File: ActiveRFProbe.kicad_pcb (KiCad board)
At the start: 2 copper layers, 53 x 19 mm, 41 parts, among them J1 Conn_01x01, J16 Conn_01x01, J17 Conn_01x01, J18 Conn_01x01, J19 Conn_01x01, J2 Conn_01x01, J20 Conn_01x01, J21 Conn_01x01, J22 Conn_01x01, J23 Conn_01x01, J24 Conn_01x01, J25 Conn_Coaxial, J3 Conn_01x01, Q1 2SC4083, Q2 2SC4083, Q3 2SC4083

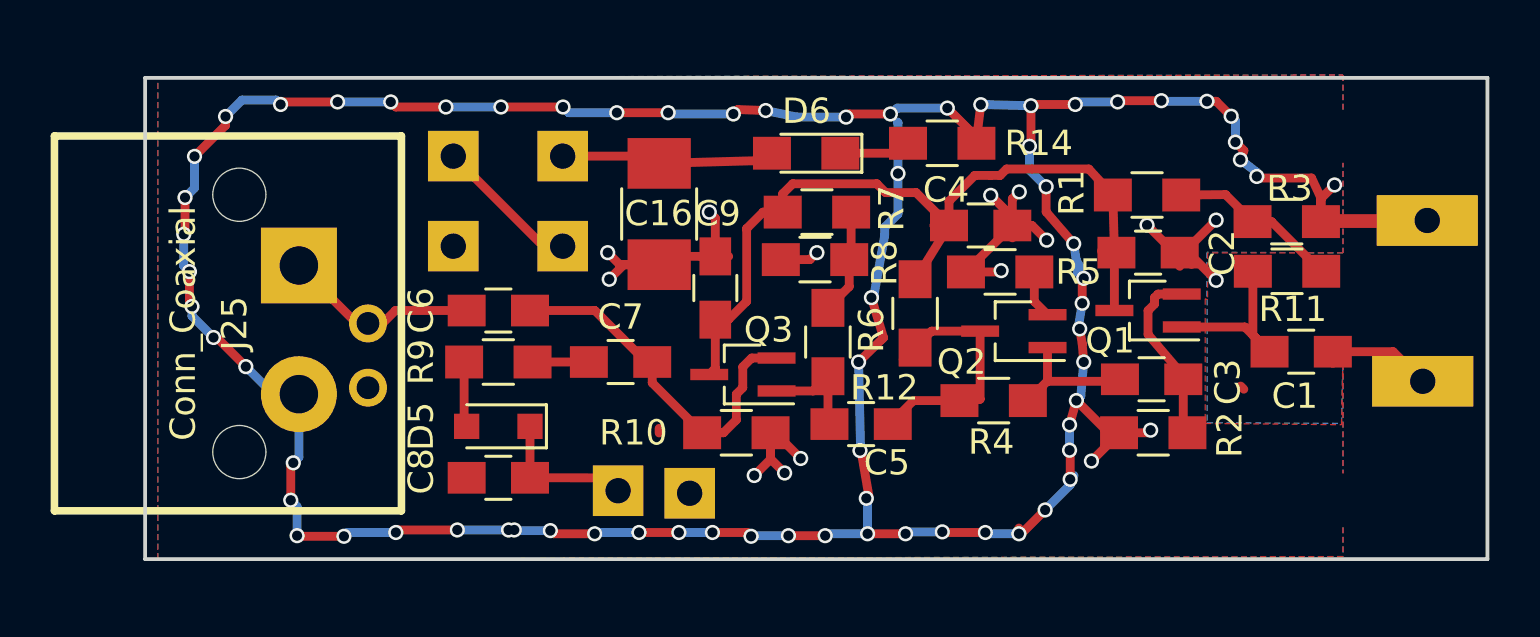
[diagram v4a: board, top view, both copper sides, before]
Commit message: Changed transistor to 2SC3357
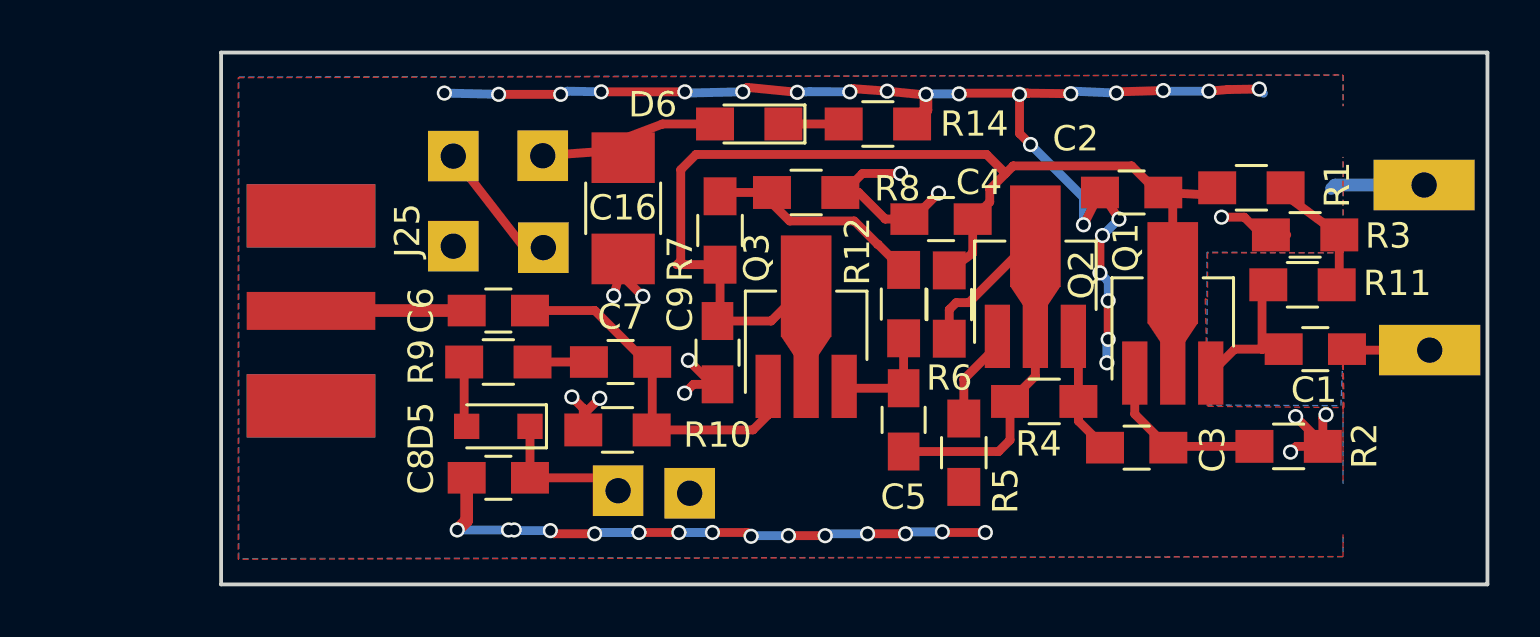
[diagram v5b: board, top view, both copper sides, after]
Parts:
- C1: value 10 nF -> 100 pF
- J25: footprint ActiveRFProbe:bnc_90_1-1337543-0_pad_combo -> ActiveRFProbe:Amphenol_RF_SMA_132289
- Q1, Q2, Q3: value 2SC4083 -> 2SC3357; footprint TO_SOT_Packages_SMD:SOT-323_SC-70_Handsoldering -> TO_SOT_Packages_SMD:SOT-89-3_Handsoldering
- moved J25 10.1 mm to (68.5, 91.2), turned to 180 degrees
- moved R5 7.28 mm to (94.3, 96.8), turned to 90 degrees
- moved R2 5.37 mm to (107.2, 96.5), turned to 0 degrees
- moved R10 4.70 mm to (80.7, 95.9), turned to 180 degrees
- moved R1 4.13 mm to (105.7, 86.3)
- moved R7 3.89 mm to (84.7, 88.0), turned to 90 degrees
- moved R12 3.34 mm to (91.9, 90.9)
- moved Q3 2.92 mm to (88.1, 92.2), turned to 90 degrees
- moved C3 2.76 mm to (101.2, 96.6)
- moved R8 2.67 mm to (88.1, 86.5), turned to 0 degrees
- moved R14 2.65 mm to (90.9, 83.8)
- moved C9 2.55 mm to (84.6, 92.8), turned to 90 degrees
- moved D6 2.53 mm to (85.9, 83.8)
- moved C2 2.46 mm to (101.0, 86.5), turned to 0 degrees
- moved R4 2.00 mm to (97.5, 94.8)
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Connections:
- Q1 pad 1: Net-(C1-Pad1) -> Net-(C3-Pad2)
- Q1 pad 2: Net-(C3-Pad2) -> +9V
- Q1 pad 3: +9V -> Net-(C1-Pad1)
- Q2 pad 1: Net-(C3-Pad1) -> Net-(Q2-Pad1)
- Q2 pad 2: Net-(Q2-Pad2) -> Net-(C5-Pad2)
- Q2 pad 3: Net-(C5-Pad2) -> Net-(C3-Pad1)
- Q3 pad 1: Net-(C5-Pad1) -> Net-(C6-Pad2)
- Q3 pad 2: Net-(C6-Pad2) -> +9V
- Q3 pad 3: +9V -> Net-(C5-Pad1)
- R5 pad 2: Net-(Q2-Pad2) -> Net-(Q2-Pad1)
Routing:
- net GND: track 188.1 -> 104.5 mm, vias 86 -> 52
- net +9V: track 34.3 -> 52.8 mm
- net Net-(C5-Pad2): track 10.4 -> 18.8 mm
- net Net-(Q2-Pad1): track 0.00 -> 5.16 mm
- net Net-(R12-Pad2): track 4.16 -> 8.83 mm
- net Net-(C1-Pad1): track 7.91 -> 5.91 mm
- net Net-(Q2-Pad2): track 1.90 -> 0.00 mm
- net Net-(R1-Pad2): track 6.78 -> 4.94 mm
- net Net-(C6-Pad1): track 7.78 -> 6.15 mm
- net Net-(C3-Pad1): track 6.34 -> 4.91 mm
- net Net-(C1-Pad2): track 4.50 -> 3.28 mm
- net Net-(C3-Pad2): track 7.99 -> 6.91 mm
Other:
- board size 53 x 19 mm -> 50 x 21 mm

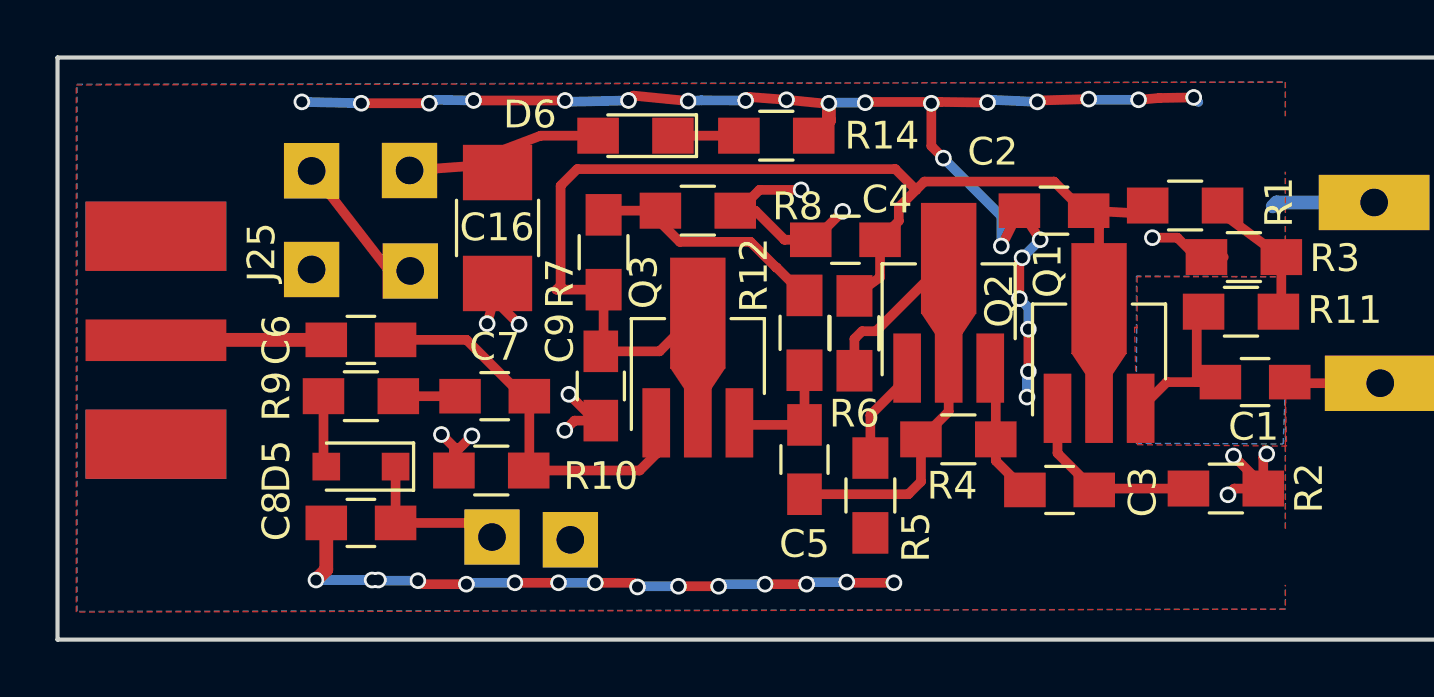
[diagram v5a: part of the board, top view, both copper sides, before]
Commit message: Fixed edge detector
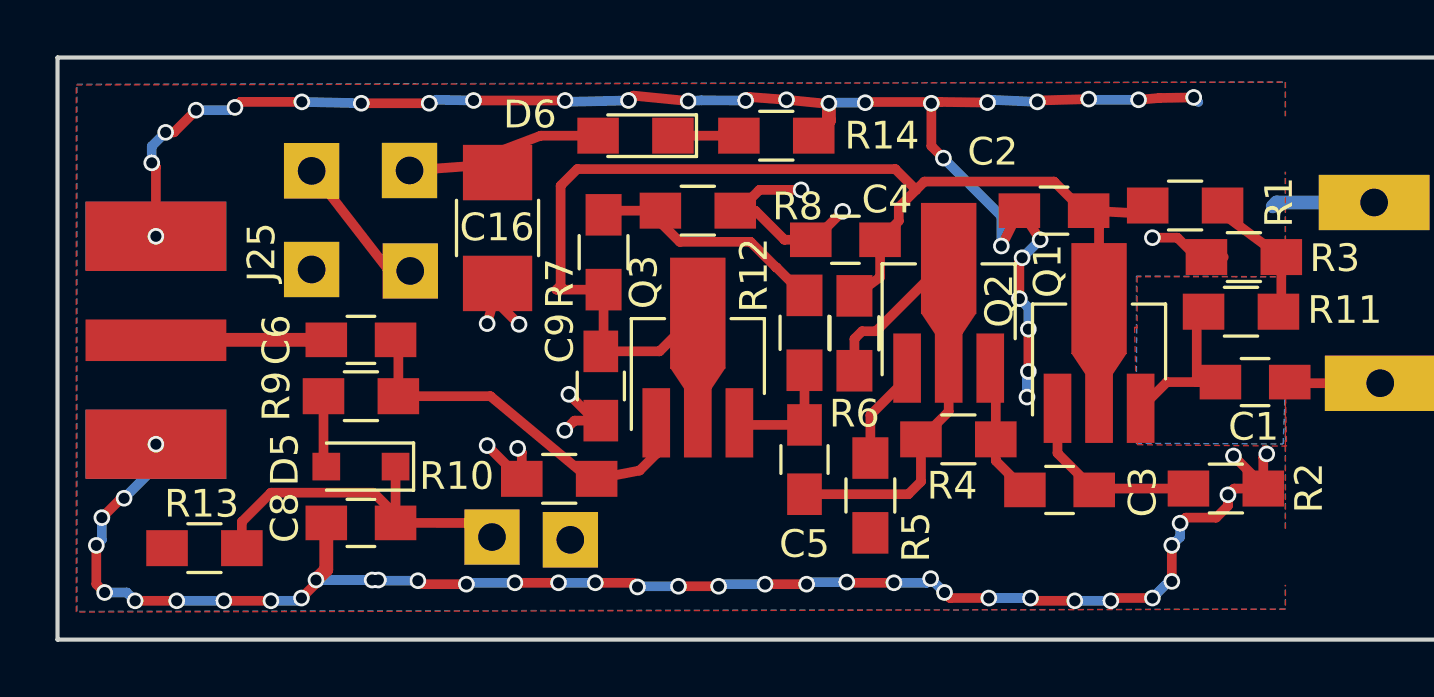
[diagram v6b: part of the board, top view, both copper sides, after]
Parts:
- removed C7: 10 nF, Capacitors_SMD:C_0805_HandSoldering
- added R13: 10k, Resistors_SMD:R_0805_HandSoldering, F.Cu at (70.3, 98.7)
- moved R10 2.47 mm to (83.1, 96.2)
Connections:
- R9 pad 2: Net-(C7-Pad1) -> Net-(C6-Pad2)
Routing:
- net GND: track 104.5 -> 143.7 mm, vias 52 -> 77
- net Net-(C8-Pad2): track 5.72 -> 13.3 mm
- net Net-(C7-Pad1): track 2.86 -> 0.00 mm

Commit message: Cleaned up the layout
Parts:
- removed R1, R3: 10k, Resistors_SMD:R_0805_HandSoldering
- removed R7, R8: 1k, Resistors_SMD:R_0805_HandSoldering
- R11: value 10k -> 47k
- R12: value 1k -> 47k
- R5: value 0R -> 47R
- R6: value 220R -> 100R
- moved J23 14.3 mm to (87.9, 83.8)
- moved J21 14.1 mm to (88.0, 98.9)
- moved J20 13.1 mm to (95.2, 98.8)
- moved J22 12.7 mm to (95.5, 83.9)
- moved R14 9.46 mm to (81.6, 85.3), turned to 180 degrees
- moved R2 4.95 mm to (102.4, 97.8), turned to 270 degrees
- moved C9 4.60 mm to (84.7, 88.2), turned to 0 degrees
- moved R6 4.31 mm to (97.8, 89.5)
- moved D6 4.21 mm to (81.7, 83.6)
- moved C5 3.95 mm to (90.7, 91.8)
- moved R12 3.77 mm to (89.3, 88.2), turned to 180 degrees
- moved C16 3.65 mm to (80.7, 90.8)
- moved Q2 3.11 mm to (94.4, 91.6)
- moved C4 2.86 mm to (96.0, 86.4)
- moved R11 2.69 mm to (105.2, 89.0), turned to 90 degrees
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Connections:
- C16 pad 2: Net-(C16-Pad2) -> +9V
- D6 pad 2: Net-(C16-Pad2) -> +9V
- J2 pad 1: Net-(C16-Pad2) -> +9V
- R11 pad 2: Net-(R1-Pad2) -> +9V
- R12 pad 2: Net-(R12-Pad2) -> +9V
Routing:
- net +9V: track 52.8 -> 75.0 mm
- net GND: track 143.7 -> 124.5 mm, vias 77 -> 70
- net Net-(R12-Pad2): track 8.83 -> 0.00 mm
- net Net-(C16-Pad2): track 8.59 -> 0.00 mm
- net Net-(C5-Pad1): track 4.35 -> 9.39 mm
- net Net-(R1-Pad2): track 4.94 -> 0.00 mm
- net Net-(C5-Pad2): track 18.8 -> 15.7 mm
- net Net-(C3-Pad1): track 4.91 -> 7.60 mm
- net Net-(C3-Pad2): track 6.91 -> 5.11 mm
- net Net-(Q2-Pad1): track 5.16 -> 4.12 mm
- net Net-(D6-Pad1): track 2.38 -> 1.77 mm
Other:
- board size 50 x 21 mm -> 49 x 22 mm
- board text added: "ACTIVE RF PROBE BY D MARKS KW4TI CC-BY-SA 4.0"
- board text removed: "RF PROBE BY D MARKS KW4TI CC-BY-SA 4.0"

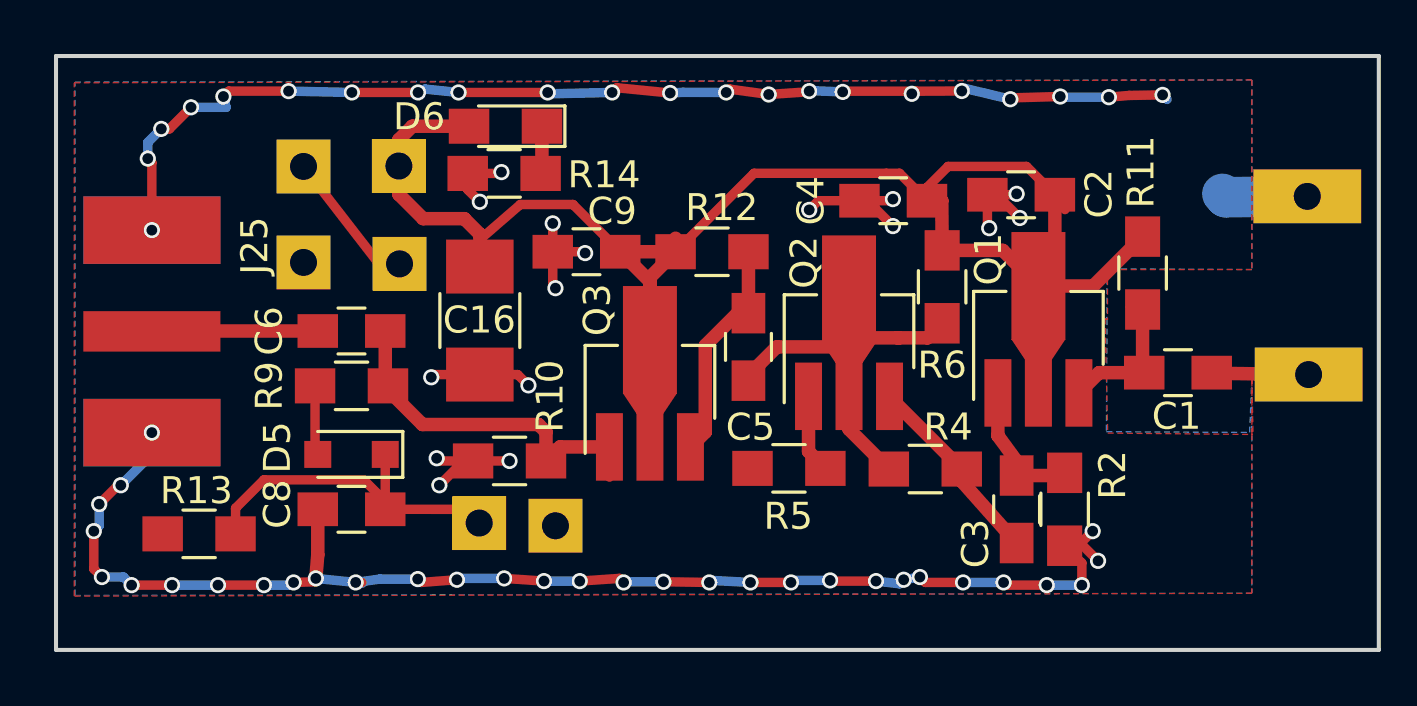
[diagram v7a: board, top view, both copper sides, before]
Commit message: Added LCSC parts, fixed symbol, added decoupling resistors
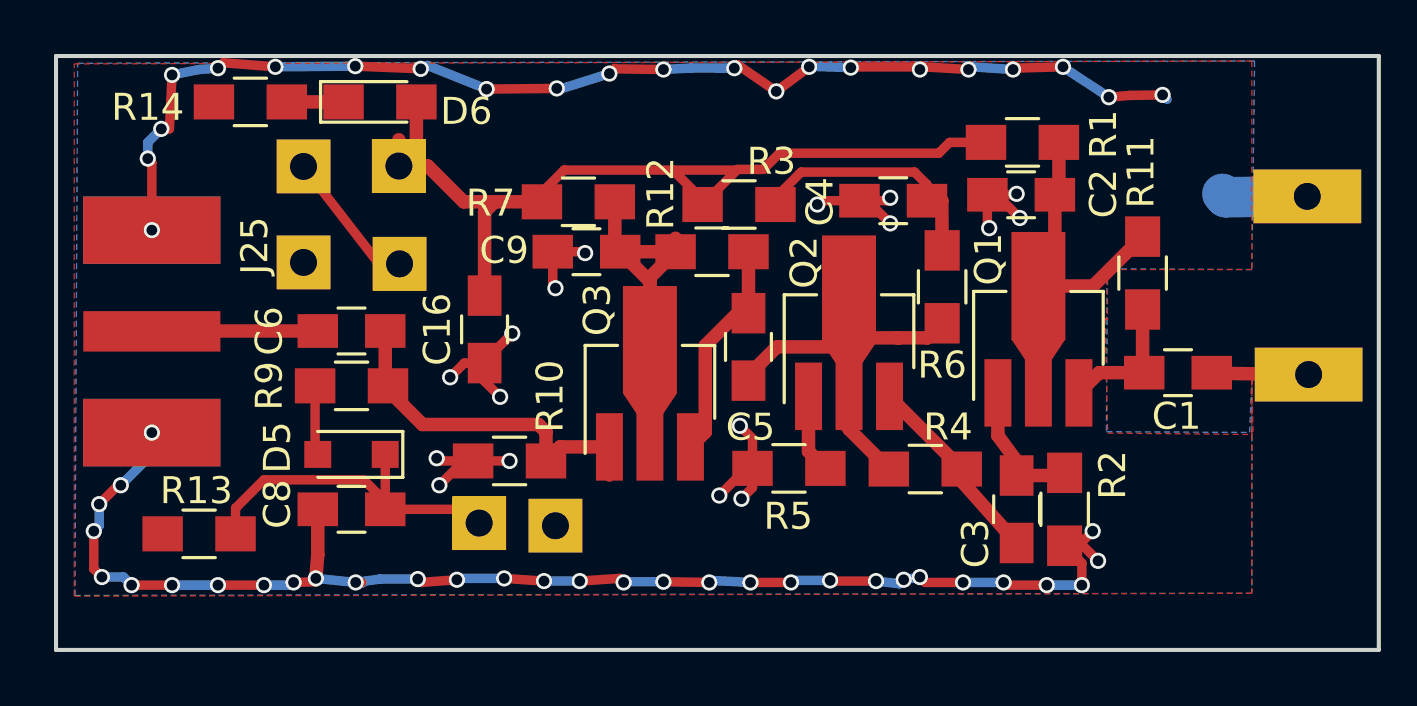
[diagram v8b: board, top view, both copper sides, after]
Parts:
- added R1: 10R, Resistors_SMD:R_0805_HandSoldering, F.Cu at (100.8, 84.2)
- added R3: 10R, Resistors_SMD:R_0805_HandSoldering, F.Cu at (90.3, 86.5)
- added R7: 10R, Resistors_SMD:R_0805_HandSoldering, F.Cu at (84.3, 86.4)
- C16: footprint Capacitors_SMD:C_1210_HandSoldering -> Capacitors_SMD:C_0805_HandSoldering
- Q1, Q2, Q3: value 2SC3357 -> 2SC1815
- R4: value 22k -> 10k
- R5: value 47R -> 22R
- moved R14 9.77 mm to (72.2, 82.7)
- moved D6 4.74 mm to (77.0, 82.7), turned to 0 degrees
- moved J22 0.94 mm to (95.5, 83.0)
- moved J23 0.82 mm to (87.9, 83.0)
- moved C16 0.37 mm to (80.9, 91.1)
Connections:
- C2 pad 2: +9V -> Net-(C2-Pad2)
- C4 pad 1: +9V -> Net-(C4-Pad1)
- C9 pad 2: +9V -> Net-(C9-Pad2)
- Q1 pad 2: +9V -> Net-(C2-Pad2)
- Q3 pad 2: +9V -> Net-(C9-Pad2)
- R11 pad 2: +9V -> Net-(C2-Pad2)
- R12 pad 2: +9V -> Net-(C9-Pad2)
- R6 pad 1: +9V -> Net-(C4-Pad1)
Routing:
- net +9V: track 75.0 -> 34.2 mm
- net Net-(C9-Pad2): track 0.00 -> 18.7 mm
- net Net-(C2-Pad2): track 0.00 -> 17.2 mm
- net Net-(C4-Pad1): track 0.00 -> 10.4 mm
- net GND: track 124.5 -> 124.6 mm, vias 70 -> 71
